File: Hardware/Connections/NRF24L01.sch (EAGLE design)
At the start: 9 parts

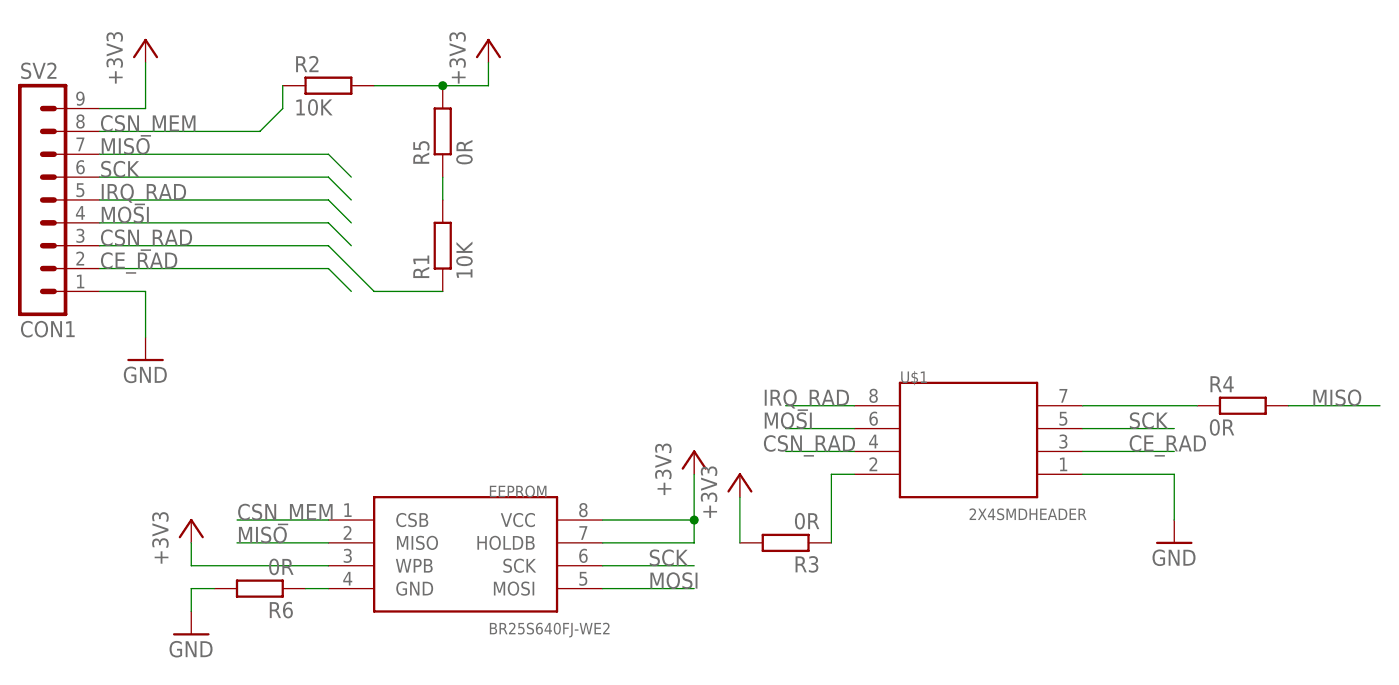
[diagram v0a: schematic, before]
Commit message: Updated PDF PCB files with Document outline mark. Fixed missing Name for NRF connector. Updated BOM to be correctly formatted.
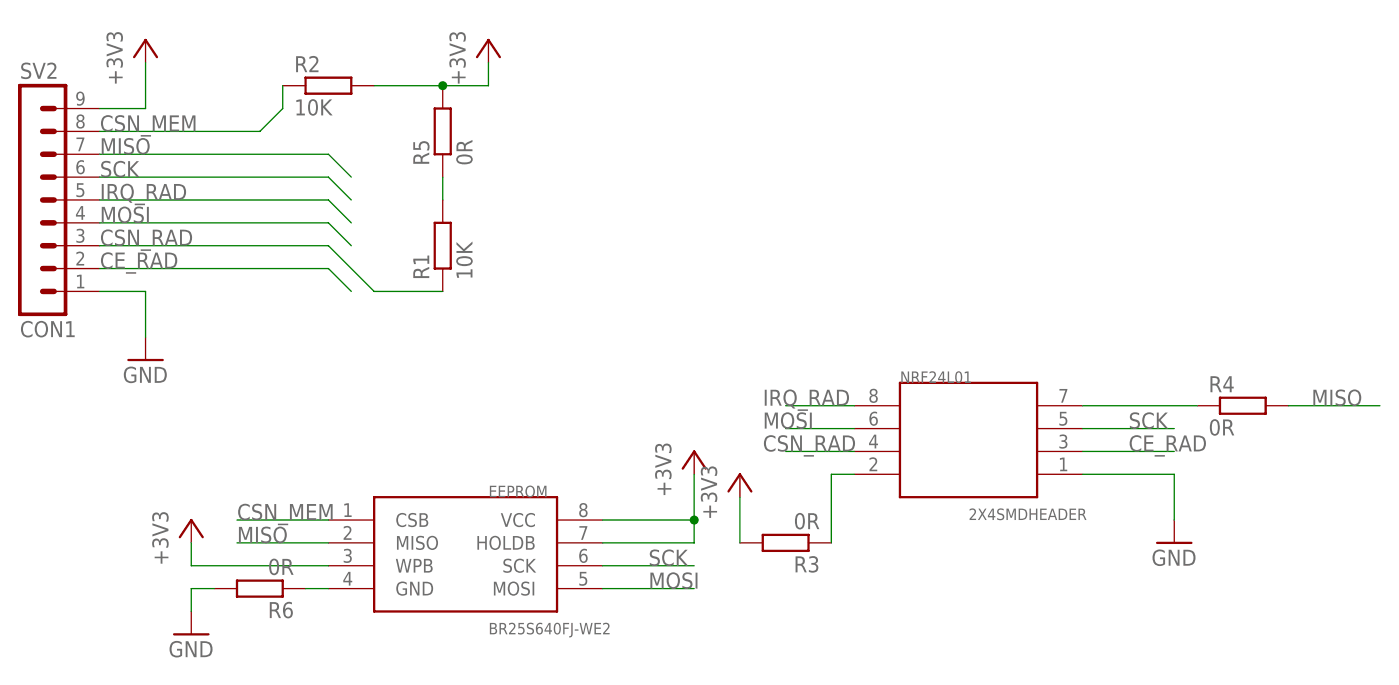
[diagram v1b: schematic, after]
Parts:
- renumbered U$1 to NRF24L01
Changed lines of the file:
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@@
 <part name="GND3" library="supply1" deviceset="GND" device=""/>
 <part name="+3V4" library="supply1" deviceset="+3V3" device=""/>
-<part name="U$1" library="Header" deviceset="2X4SMDHEADER" device=""/>
+<part name="NRF24L01" library="Header" deviceset="2X4SMDHEADER" device=""/>
 <part name="GND4" library="supply1" deviceset="GND" device=""/>
 <part name="+3V5" library="supply1" deviceset="+3V3" device=""/>
@@
 <instance part="GND3" gate="1" x="10.16" y="5.08"/>
 <instance part="+3V4" gate="G$1" x="10.16" y="17.78"/>
-<instance part="U$1" gate="G$1" x="96.52" y="27.94"/>
+<instance part="NRF24L01" gate="G$1" x="96.52" y="27.94"/>
 <instance part="GND4" gate="1" x="119.38" y="15.24"/>
 <instance part="+3V5" gate="G$1" x="71.12" y="22.86"/>
@@
 </segment>
 <segment>
-<pinref part="U$1" gate="G$1" pin="1"/>
+<pinref part="NRF24L01" gate="G$1" pin="1"/>
 <pinref part="GND4" gate="1" pin="GND"/>
 <wire x1="109.22" y1="22.86" x2="119.38" y2="22.86" width="0.1524" layer="91"/>
@@
 </segment>
 <segment>
-<pinref part="U$1" gate="G$1" pin="6"/>
+<pinref part="NRF24L01" gate="G$1" pin="6"/>
 <wire x1="83.82" y1="27.94" x2="76.2" y2="27.94" width="0.1524" layer="91"/>
 <label x="73.66" y="27.94" size="1.778" layer="95"/>
@@
 </segment>
 <segment>
-<pinref part="U$1" gate="G$1" pin="5"/>
+<pinref part="NRF24L01" gate="G$1" pin="5"/>
 <wire x1="109.22" y1="27.94" x2="119.38" y2="27.94" width="0.1524" layer="91"/>
 <label x="114.3" y="27.94" size="1.778" layer="95"/>
@@
 </segment>
 <segment>
-<pinref part="U$1" gate="G$1" pin="4"/>
+<pinref part="NRF24L01" gate="G$1" pin="4"/>
 <wire x1="83.82" y1="25.4" x2="76.2" y2="25.4" width="0.1524" layer="91"/>
 <label x="73.66" y="25.4" size="1.778" layer="95"/>
@@
 </segment>
 <segment>
-<pinref part="U$1" gate="G$1" pin="3"/>
+<pinref part="NRF24L01" gate="G$1" pin="3"/>
 <wire x1="109.22" y1="25.4" x2="119.38" y2="25.4" width="0.1524" layer="91"/>
 <label x="114.3" y="25.4" size="1.778" layer="95"/>
@@
 </segment>
 <segment>
-<pinref part="U$1" gate="G$1" pin="8"/>
+<pinref part="NRF24L01" gate="G$1" pin="8"/>
 <wire x1="83.82" y1="30.48" x2="76.2" y2="30.48" width="0.1524" layer="91"/>
 <label x="73.66" y="30.48" size="1.778" layer="95"/>
@@
 <pinref part="R4" gate="G$1" pin="1"/>
 <wire x1="121.92" y1="30.48" x2="109.22" y2="30.48" width="0.1524" layer="91"/>
-<pinref part="U$1" gate="G$1" pin="7"/>
+<pinref part="NRF24L01" gate="G$1" pin="7"/>
 </segment>
 </net>
 <net name="N$1" class="0">
 <segment>
-<pinref part="U$1" gate="G$1" pin="2"/>
+<pinref part="NRF24L01" gate="G$1" pin="2"/>
 <wire x1="83.82" y1="22.86" x2="81.28" y2="22.86" width="0.1524" layer="91"/>
 <wire x1="81.28" y1="22.86" x2="81.28" y2="15.24" width="0.1524" layer="91"/>
